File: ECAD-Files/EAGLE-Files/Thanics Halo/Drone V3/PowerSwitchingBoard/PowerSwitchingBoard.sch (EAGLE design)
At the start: 252 parts, among them J1 ESC_CONTACTS, J3 62674-301121ALF, J4 B3B-ZR-SM4, J5 B3B-ZR-SM4, J6 B3B-ZR-SM4, Q1 500mA/300V, Q19 500mA/300V, Q2 500mA/300V, Q20 IRLR8726, Q21 IRLR8726, Q22 500mA/300V, Q23 IRLR8726, Q24 IRLR8726, Q25 500mA/300V, Q26 IRLR8726, Q27 IRLR8726, Q28 500mA/300V, Q29 IRLR8726, Q3 500mA/300V, Q30 IRLR8726, Q31 500mA/300V, Q32 IRLR8726, Q33 IRLR8726, Q34 500mA/300V, Q35 IRLR8726, Q36 IRLR8726, Q37 500mA/300V, Q38 IRLR8726, Q39 IRLR8726, Q4 IRLR8726, Q40 500mA/300V, Q41 IRLR8726, Q42 IRLR8726, Q43 500mA/300V, Q44 IRLR8726, Q45 IRLR8726, Q5 IRLR8726, Q6 IRLR8726, Q7 IRLR8726, Q8 IRLR8726, Q9 IRLR8726, U1 TPS65261RHBR, U10 MEGA8-AI, U11 MEGA8-AI, U2 74HC4052PW, U3 74HC4052PW, U4 DRV8313, U5 DRV8313, U6 DRV8313, U7 STM32F103RCT6LQFP-64-M, U8 MEGA8-AI, U9 MEGA8-AI, X1 16MHz, X3 16MHz, X4 16MHz, X5 16MHz, X6 8MHz

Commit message: Created TOF Altimeter Board v1, and made power board 4 layers
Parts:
- removed L3: 4.7uH, 4.7uH-inductor:DFE252012P-4R7M=P2"
- removed R16: 20k, 20k-resistor:RC0402FR-0720KLRC0402N-M
- removed U1: TPS65261RHBR, tps65261:TPS65261RHBR
- added C52, C54, C55: 22uF, 22uF X5R Ceramic Capacitor:GRM21BR60J226ME39L
- added C53, C62, C63, C64, C65, C66, C67, C68, C69, C70, C71, C72, C73, C74, C75: 0.1uF, 0.1uF-capacitor-0402:0402ZD104KAT2A0402-M
- added C56: 2.2nF, thanics_robotics:2200PF_CAPACITOR
- added C57, C58, C59, C60, C61: 22uF, thanics_robotics:CL32A226MAJNNNE
- added D13, D14: SSB44-E3/52T, ssb44-schottky:SSB44-E3/52TDIODE_DO214AA_MBRS-M
- added F1, F2: 0ZRB0400FF1A, ptc-fuse:0ZRB0400FF1A
- added R39: 2.2k, 2.2k-resistor:RC0603JR-072K2LRC0603N-M
- added R42: 10k (1%), 10k-resistor(0603):RC0603JR-0710KLRC0603N-M
- added R43: 100k, 100k-resistor:RC0603JR-07100KLRC0603N-M
- added R44: 47k, 47k-resistor:RC0603JR-0747KLRC0603N-M
- added U12, U13: AOZ1284, thanics_robotics:AOZ1284
- added U14: SN74LVC1G373DCKRDCK6-M, d-latch:SN74LVC1G373DCKRDCK6-M
- C13: value 10uF -> 22uF; device thanics_robotics:10UF_CAPACITOR -> 22uF X5R Ceramic Capacitor:GRM21BR60J226ME39L
- C15, C16: value 0.1uF -> 22uF; device 0.1uF-capacitor-0402:0402ZD104KAT2A0402-M -> 22uF X5R Ceramic Capacitor:GRM21BR60J226ME39L
- C17: value 1uF -> 2.2nF; device 1uF X7R Ceramic Capacitor:CC0805KKX7R7BB105 -> thanics_robotics:2200PF_CAPACITOR
- C18, C2: value 10uF -> 1nF; device thanics_robotics:10UF_CAPACITOR -> 1000pF-capacitor:GRM155R60J102KA01DG-155-M
- C19, C20, C21, C25, C8: device 22uF X5R Ceramic Capacitor:GRM21BR60J226ME39L -> thanics_robotics:CL32A226MAJNNNE
- C22, C23, C24: value 2.2nF -> 22uF; device thanics_robotics:2200PF_CAPACITOR -> thanics_robotics:CL32A226MAJNNNE
- C48: value 470uF -> 22uF; device 470uF-capacitor:UWT1E471MNL1GSPCAP_10X10-ELECT-M -> thanics_robotics:CL32A226MAJNNNE
- L1, L2: value 4.7uH -> 10uH; device 4.7uH-inductor:DFE252012P-4R7M=P2" -> thanics_robotics:PA4341.103
- R10: value 10k -> 52.3k (1%); device 10k-resistor(0603):RC0603JR-0710KLRC0603N-M -> thanics_robotics:RC0402FR-0752K3L
- R11: value 10k -> 100k; device 10k-resistor(0603):RC0603JR-0710KLRC0603N-M -> 100k-resistor:RC0603JR-07100KLRC0603N-M
- R13: value 73.2k -> 100k; device 45.3k-resistor:RC0402FR-0745K3LRC0402N-M -> 100k-resistor:RC0603JR-07100KLRC0603N-M
- R14: value 20k -> 1k; device 20k-resistor:RC0402FR-0720KLRC0402N-M -> 1k-resistor:RC0603JR-071KLRC0603N-M
- R15: value 20k -> 100k; device 20k-resistor:RC0402FR-0720KLRC0402N-M -> 100k-resistor:RC0603JR-07100KLRC0603N-M
- R2: value 10k -> 31.6k (1%); device 10k-resistor(0603):RC0603JR-0710KLRC0603N-M -> thanics_robotics:RC0402FR-0731K6L
- R7: value 45.3k -> 31.6k (1%); device 73.2k-resistor:RMCF0402FT73K2STA_RMCF0402-M -> thanics_robotics:RC0402FR-0731K6L
- R8: value 73.2k -> 10k (1%); device 45.3k-resistor:RC0402FR-0745K3LRC0402N-M -> 10k-resistor(0603):RC0603JR-0710KLRC0603N-M
- R9: value 20k -> 47k; device 20k-resistor:RC0402FR-0720KLRC0402N-M -> 47k-resistor:RC0603JR-0747KLRC0603N-M
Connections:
- removed net +1V8: C25.22, J3.77, J3.88, L1.1, R9.11
- removed net N$16: C15.2, U1.BST1
- removed net N$20: C14.2, L1.2, U1.LX2
- removed net N$23: C17.22, U1.V7V
- removed net N$26: R16.11, U1.COMP2
- removed net N$27: C22.2, R16.22
- removed net N$28: R15.22, U1.COMP1
- removed net N$29: C23.1, R15.11
- new net EN: R11.22, R15.22, U12.EN, U13.EN, U14.Q
- new net N$49: C53.1, U12.BS
- new net N$50: C53.2, D13.12, L1.1, U12.LX
- new net N$51: R42.11, R7.11, U12.FB
- new net N$52: R43.11, U12.FSW
- new net PWR_EN: J3.1818, R13.22, U14.!OE, U14.D
- new net V2FUSED: C16.22, C64.2, F2.2, U13.VIN
- new net VFUSED: C55.22, C63.2, F1.2, U12.VIN
- new net V_LATCH: R11.11, R13.11, R14.11, R15.11, R39.22, U14.LE, U14.VCC
- net +3V3: now also C52.22, C54.11, L1.2, R7.22; no longer C19.22, L2.2, R7.11
- net +5V: now also C13.22, C15.11, C62.1, C66.2, C67.1, C69.2, C70.1, C72.2, C73.1, C75.2, L2.2, R10.22; no longer C20.22, C21.22, L3.2, R8.22
- net BOOT0: no longer J3.1818
- net GND: now also C13.11, C15.22, C16.11, C18.11, C19.1, C2.11, C20.1, C21.1, C23.1, C24.1, C25.1, C48.2, C52.11, C54.22, C55.11, C57.2, C58.2, C59.2, C60.2, C61.2, C62.2, C63.1, C64.1, C65.2, C66.1, C67.2, C68.2, C69.1, C70.2, C71.2, C72.1, C73.2, C74.2, C75.1, C8.1, D13.21, D14.21, J3.77, J3.88, R14.22, R2.11, R42.22, R43.22, R44.22, R8.22, R9.22, U12.GND, U13.GND, U14.GND; no longer C13.1, C17.11, C18.1, C19.11, C2.1, C20.11, C21.11, C23.2, C24.2, C25.11, C48.22, C8.22, R10.22, R11.22, R13.11, R2.22, U1.AGND, U1.EPAD, U1.MODE, U1.PGND1, U1.PGND2, U1.PGND3
- net N$11: now also C2.22, U12.SS; no longer C14.1, U1.BST2
- net N$12: now also C14.1, U13.BS; no longer R14.22, U1.COMP3
- net N$13: now also C14.2, D14.12, L2.1, U13.LX; no longer R2.11, R9.22, U1.FB2
- net N$14: now also R10.11, R8.11, U13.FB; no longer R13.22, U1.ROSC
- net N$15: now also R44.11, U13.FSW; no longer C15.1, L2.1, U1.LX1
- net N$17: now also C17.2, U13.COMP; no longer R10.11, R7.22, U1.FB1
- net N$18: now also C17.1, R9.11; no longer C24.1, R14.11
- net N$19: now also C18.22, U13.SS; no longer C16.1, L3.1, U1.LX3
- net N$2: now also C56.2, U12.COMP; no longer C16.2, U1.BST3
- net N$3: now also C56.1, R2.22; no longer R11.11, R8.11, U1.FB3
- net RST1: now also C68.1
- net RST2: now also C65.1
- net RST3: now also C71.1
- net RST4: now also C74.1
- net VDD: now also C19.2, C20.2, C21.2, C22.2, C23.2, C24.2, C25.2, C48.1, C57.1, C58.1, C59.1, C60.1, C61.1, C8.2, F1.1, F2.1, R39.11; no longer C13.2, C18.2, C2.2, C48.11, C8.11, U1.PVIN1, U1.PVIN2, U1.PVIN3, U1.VIN
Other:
- note added: "*Notes: Compensation networks are calculated with 2A load and 25kHz crossover frequency U12 Fsw = 500kHz U13 Fsw = 1MHz"
- note removed: "Triple Buck Converter -5V -3V3 -1V8 **18V MAX INPUT (3-4S LiPo ONLY)**"

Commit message: finished power board v1.2
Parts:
- removed R42: 10k (1%), 10k-resistor(0603):RC0603JR-0710KLRC0603N-M
- removed R43: 100k, 100k-resistor:RC0603JR-07100KLRC0603N-M
- removed R44: 47k, 47k-resistor:RC0603JR-0747KLRC0603N-M
- removed U13: AOZ1284, thanics_robotics:AOZ1284
- added R16: 10.2k, thanics-resistor:RC0402FR-0710K2L
- added U1: TPS54331DRD8-M, tps54331:TPS54331DRD8-M
- C13, C15, C16: device 22uF X5R Ceramic Capacitor:GRM21BR60J226ME39L -> thanics_robotics:CL32A226MAJNNNE
- C14: value 0.1uF -> 10nF; device 0.1uF-capacitor-0402:0402ZD104KAT2A0402-M -> thanics_robotics:10NF_CAPACITOR
- C17: value 2.2nF -> 22uF; device thanics_robotics:2200PF_CAPACITOR -> thanics_robotics:CL32A226MAJNNNE
- C18: device 1000pF-capacitor:GRM155R60J102KA01DG-155-M -> thanics-capacitor:GRM155R60J102KA01D
- C2: value 1nF -> 22uF; device 1000pF-capacitor:GRM155R60J102KA01DG-155-M -> thanics_robotics:CL32A226MAJNNNE
- C26: value 10uF -> 0.1uF; device 10uF X5R Ceramic Capacitor:GRM21BR60J106ME19L -> 0.1uF-capacitor-0402:0402ZD104KAT2A0402-M
- C44: value 10uF -> 43pF; device 10uF X5R Ceramic Capacitor:GRM21BR60J106ME19L -> thanics-capacitor:CL10C430JB8NNNC
- C47: value 10uF -> 22uF; device 10uF X5R Ceramic Capacitor:GRM21BR60J106ME19L -> thanics-capacitor:CL21A226MOCLRNC
- C52: value 22uF -> 10nF; device 22uF X5R Ceramic Capacitor:GRM21BR60J226ME39L -> thanics_robotics:10NF_CAPACITOR
- C53: value 0.1uF -> 2.2nF; device 0.1uF-capacitor-0402:0402ZD104KAT2A0402-M -> thanics_robotics:2200PF_CAPACITOR
- C54: value 22uF -> 0.1uF; device 22uF X5R Ceramic Capacitor:GRM21BR60J226ME39L -> 0.1uF-capacitor-0402:0402ZD104KAT2A0402-M
- C55: value 22uF -> 43pF; device 22uF X5R Ceramic Capacitor:GRM21BR60J226ME39L -> thanics-capacitor:CL10C430JB8NNNC
- C56: value 2.2nF -> 22uF; device thanics_robotics:2200PF_CAPACITOR -> thanics-capacitor:CL21A226MOCLRNC
- C63, C64: value 0.1uF -> 22uF; device 0.1uF-capacitor-0402:0402ZD104KAT2A0402-M -> thanics-capacitor:CL21A226MOCLRNC
- R10: value 52.3k (1%) -> 10.2k; device thanics_robotics:RC0402FR-0752K3L -> thanics-resistor:RC0402FR-0710K2L
- R2: value 31.6k (1%) -> 3.24k; device thanics_robotics:RC0402FR-0731K6L -> thanics-resistor:RMCF0603FT3K24
- R7: value 31.6k (1%) -> 28.7k; device thanics_robotics:RC0402FR-0731K6L -> thanics-resistor:RC0402FR-0728K7L
- R8: value 10k (1%) -> 1.96k; device 10k-resistor(0603):RC0603JR-0710KLRC0603N-M -> thanics-resistor:RC0603FR-071K96L
- R9: value 47k -> 39.2k; device 47k-resistor:RC0603JR-0747KLRC0603N-M -> thanics-resistor:RC0402FR-0739K2L
- U12: value AOZ1284 -> TPS54331DRD8-M; device thanics_robotics:AOZ1284 -> tps54331:TPS54331DRD8-M
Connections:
- removed net N$49: C53.1, U12.BS
- removed net N$50: C53.2, D13.12, L1.1, U12.LX
- removed net N$51: R42.11, R7.11, U12.FB
- removed net N$52: R43.11, U12.FSW
- new net N$16: C26.1, U1.BOOT
- new net N$20: R16.1, R2.2, U12.VSENSE
- net +3V3: now also C56.1, C63.1, R16.2; no longer C52.22, C54.11, R7.22
- net +5V: now also C47.1, C64.1, R10.2; no longer C13.22, C15.11, R10.22
- net EN: now also R15.11, U1.EN; no longer R15.22, U13.EN
- net GND: now also C13.1, C14.1, C15.1, C16.1, C17.2, C18.2, C2.2, C44.2, C47.2, C52.1, C53.1, C55.2, C56.2, C63.2, C64.2, R2.1, R8.1, U1.GND; no longer C13.11, C15.22, C16.11, C18.11, C2.11, C26.11, C44.11, C47.11, C52.11, C54.22, C55.11, C63.1, C64.1, R2.11, R42.22, R43.22, R44.22, R8.22, R9.22, U13.GND
- net N$11: now also C52.2; no longer C2.22
- net N$12: now also C54.1, U12.BOOT; no longer C14.1, U13.BS
- net N$13: now also C44.1, R9.2, U1.COMP; no longer C14.2, D14.12, L2.1, U13.LX
- net N$14: now also C18.1, R9.1; no longer R10.11, R8.11, U13.FB
- net N$15: now also C14.2, U1.SS; no longer R44.11, U13.FSW
- net N$17: now also C26.2, D14.12, L2.1, U1.PH; no longer C17.2, U13.COMP
- net N$18: now also C54.2, D13.12, L1.1, U12.PH; no longer C17.1, R9.11
- net N$19: now also R10.1, R8.2, U1.VSENSE; no longer C18.22, U13.SS
- net N$2: now also C55.1, R7.2; no longer C56.2
- net N$3: now also C53.2, R7.1; no longer C56.1, R2.22
- net V2FUSED: now also C17.1, U1.VIN; no longer C16.22, C64.2, U13.VIN
- net VDD: now also C13.2, C15.2, C16.2; no longer C26.22, C44.22, C47.22
- net VFUSED: now also C2.1; no longer C55.22, C63.2
- net V_LATCH: now also R15.22; no longer R15.11
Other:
- note removed: "*Notes: Compensation networks are calculated with 2A load and 25kHz crossover frequency U12 Fsw = 500kHz U13 Fsw = 1MHz"
- moved on the sheet: C54, C56, D13, D14, L1, L2, R15

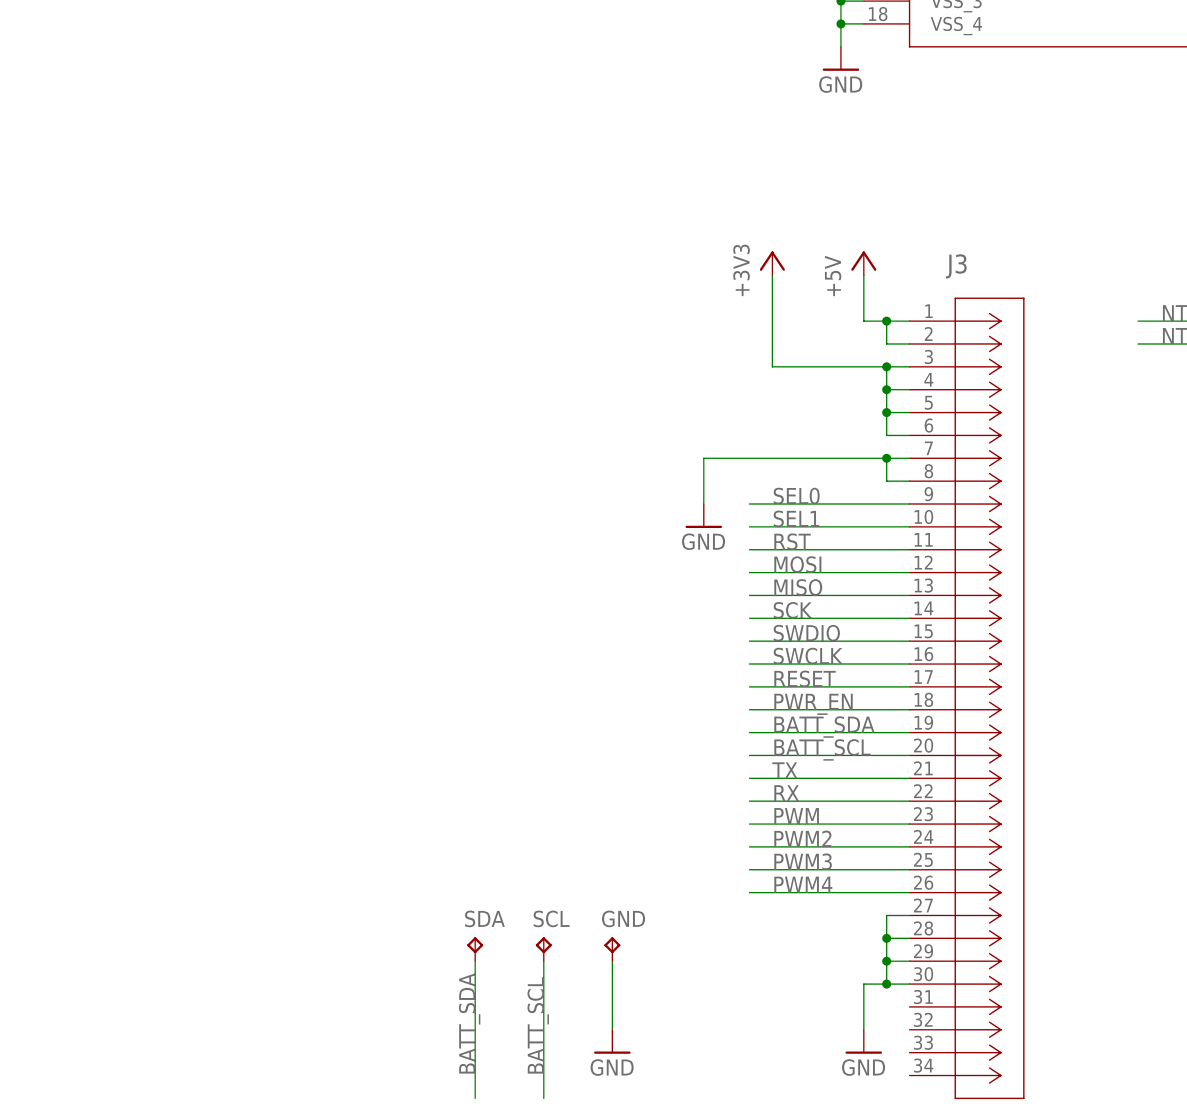
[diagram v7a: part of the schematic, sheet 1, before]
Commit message: About to remove touchscreen from controller board
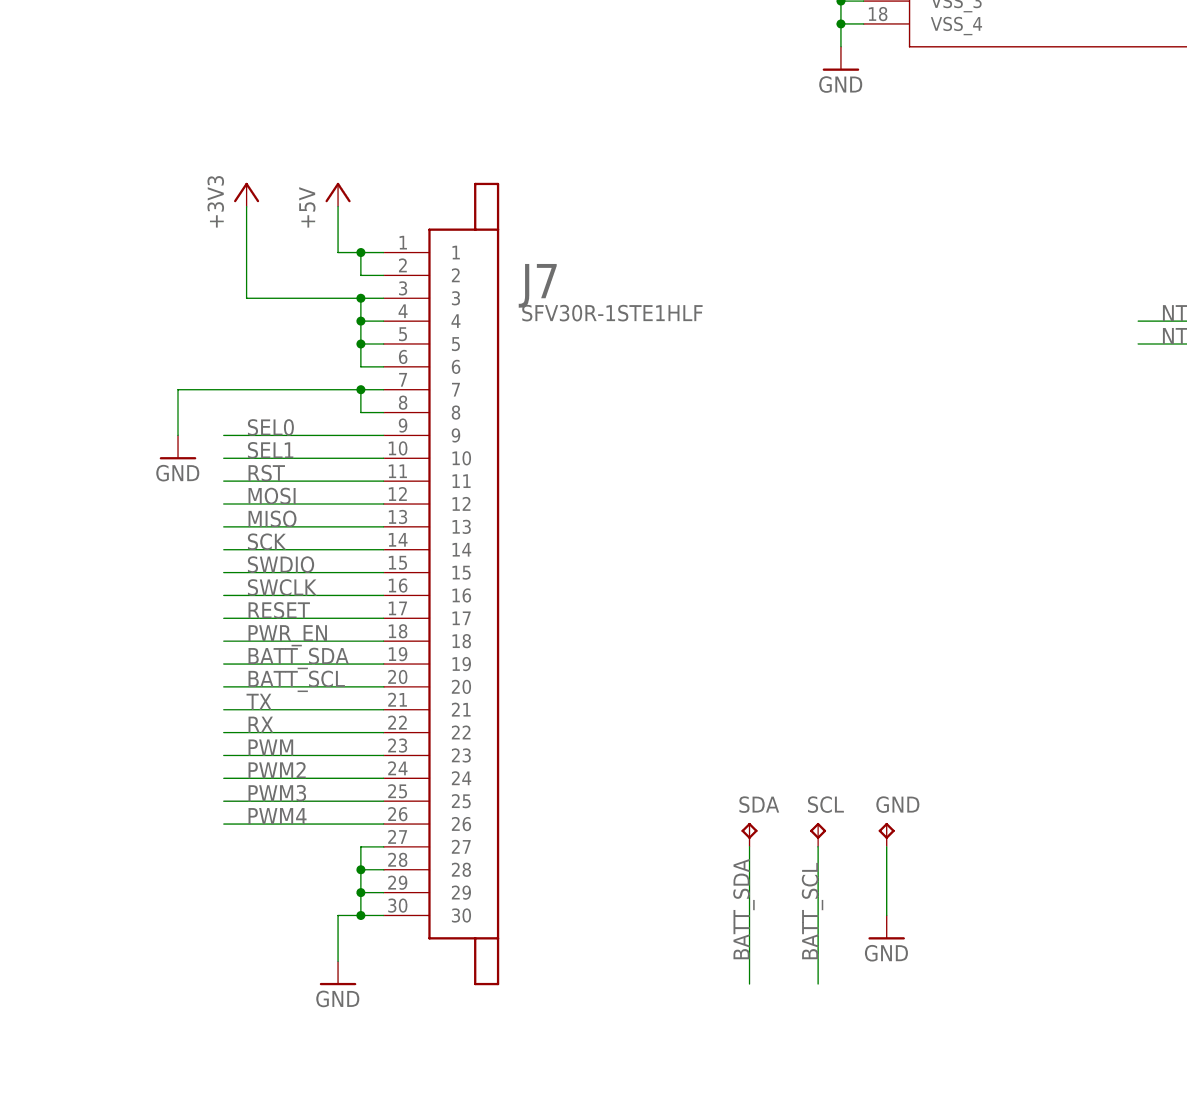
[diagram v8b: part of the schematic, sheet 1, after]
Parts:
- removed J3: 62674-301121ALF, 30pin_ffc_connector:62674-301121ALF
- added J7: SFV30R-1STE1HLF, thanics-connector:SFV30R-1STE1HLF
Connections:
- net +3V3: now also J7.3, J7.4, J7.5, J7.6; no longer J3.33, J3.44, J3.55, J3.66
- net +5V: now also J7.1, J7.2; no longer J3.11, J3.22
- net BATT_SCL: now also J7.20; no longer J3.2020
- net BATT_SDA: now also J7.19; no longer J3.1919
- net GND: now also J7.27, J7.28, J7.29, J7.30, J7.7, J7.8; no longer J3.2727, J3.2828, J3.2929, J3.3030, J3.77, J3.88
- net MISO: now also J7.13; no longer J3.1313
- net MOSI: now also J7.12; no longer J3.1212
- net PWM: now also J7.23; no longer J3.2323
- net PWM2: now also J7.24; no longer J3.2424
- net PWM3: now also J7.25; no longer J3.2525
- net PWM4: now also J7.26; no longer J3.2626
- net PWR_EN: now also J7.18; no longer J3.1818
- net RESET: now also J7.17; no longer J3.1717
- net RST: now also J7.11; no longer J3.1111
- net RX: now also J7.22; no longer J3.2222
- net SCK: now also J7.14; no longer J3.1414
- net SEL0: now also J7.9; no longer J3.99
- net SEL1: now also J7.10; no longer J3.1010
- net SWCLK: now also J7.16; no longer J3.1616
- net SWDIO: now also J7.15; no longer J3.1515
- net TX: now also J7.21; no longer J3.2121
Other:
- moved on the sheet: GND, SCL, SDA
